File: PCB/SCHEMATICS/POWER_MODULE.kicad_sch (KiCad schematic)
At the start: 44 parts, among them Q1 PMOS, U1 C7433, U2 AMS1117-3.3, U4 AMS1117-3.3

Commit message: Added stm
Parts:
- U9: footprint (none) -> footprints:18650_Holder_SMD
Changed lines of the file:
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@@
       (effects (font (size 1.27 1.27)))
     )
-    (property "Footprint" "" (at 52.07 151.13 0)
+    (property "Footprint" "footprints:18650_Holder_SMD" (at 52.07 151.13 0)
       (effects (font (size 1.27 1.27)) hide)
     )

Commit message: Updated schematics
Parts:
- removed U9: ~, footprints:18650_Holder_SMD, symbol Battery holder:18650_holder
- Q1: footprint (none) -> footprint:SOT-23-3_L3.0-W1.6-P1.90-LS2.8-BR; PART  C20917 -> C2959854; Unit Price 0.0864 -> 0.0851
- R1, R14, R15, R4, R5, R7: PART  C17168 -> C17168
- R12: footprint (none) -> footprint:R1206
- R40: value Value: Value: Value: Value: Value: Value: 510k -> Value: Value: Value: 510k; footprint (none) -> footprint:R0402
- TP4054-42-SOT25R: footprint LIB_TP4054-42-SOT25-R:SOT95P280X100-5N -> footprint:SOT-23-5_L3.0-W1.7-P0.95-LS2.8-BL
- U1: footprint Package_TO_SOT_SMD:TSOT-23-5 -> footprint:SOIC-8_L4.9-W3.9-P1.27-LS6.0-BL
- U2, U4: footprint LIB_AMS1117-3.3:SOT229P700X180-4N -> footprint:SOT-223-4_L6.5-W3.5-P2.30-LS7.0-BR; PART  U2 -> C369933; Unit Price 0.0627 -> 0.0646
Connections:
- net GND: no longer D5.1 (K), Q1.3 (S), R10.2, R11.2, R8.1, R9.1, U1.2 (V-), U1.5 (V+)
- new net: D5.1 (K), Q1.3 (S), R10.2, R11.2, R8.1, R9.1, U1.2 (V-), U1.5 (V+)
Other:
- moved on the sheet: D3, D5, Q1, R10, R11, R12, R13, R14, R15, R40, R8, R9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

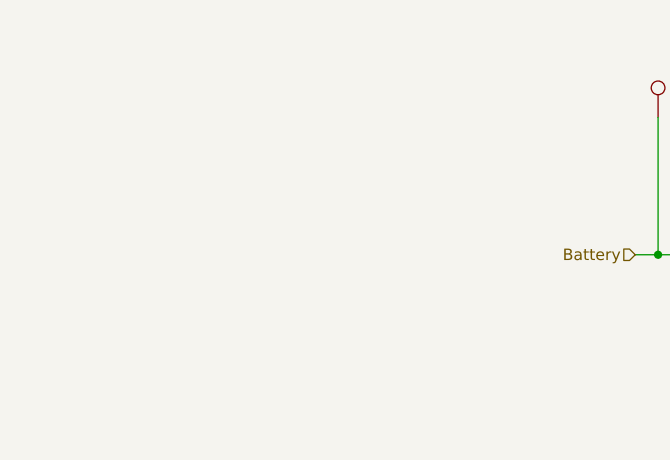
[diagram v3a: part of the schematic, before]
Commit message: Added battery
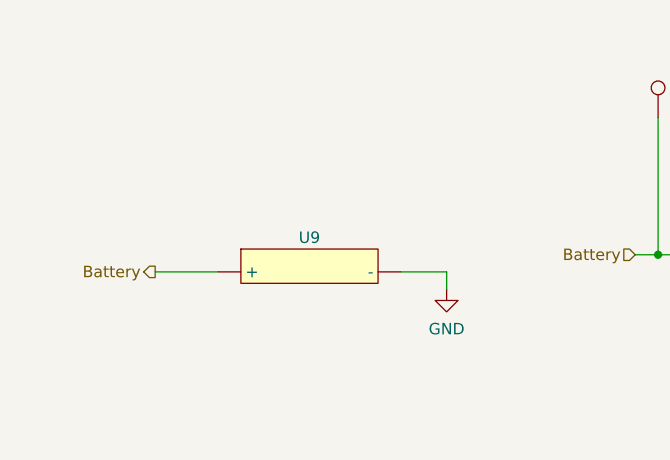
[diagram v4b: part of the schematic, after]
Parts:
- added U9: ~, footprints:18650_Holder_SMD, symbol Battery:18650
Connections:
- net Battery: now also U9. (-)
- net GND: now also U9. (-)
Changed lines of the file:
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@@
+    (stroke (width 0) (type default))
+  )
+  (wire (pts (xy 60.325 144.78) (xy 60.325 146.685))
     (stroke (width 0) (type default))
   )
@@
     (stroke (width 0) (type default))
   )
+  (wire (pts (xy 55.245 144.78) (xy 60.325 144.78))
+    (stroke (width 0) (type default))
+  )
   (wire (pts (xy 122.555 124.46) (xy 139.7 124.46))
     (stroke (width 0) (type default))
@@
   )
   (wire (pts (xy 157.48 64.77) (xy 163.83 64.77))
+    (stroke (width 0) (type default))
+  )
+  (wire (pts (xy 27.94 144.78) (xy 34.925 144.78))
     (stroke (width 0) (type default))
   )
@@
     (effects (font (size 1.27 1.27)) (justify left))
   )
+  (hierarchical_label "Battery" (shape output) (at 27.94 144.78 180) (fields_autoplaced)
+    (effects (font (size 1.27 1.27)) (justify right))
+  )
   (hierarchical_label "5V" (shape input) (at 63.5 24.13 90) (fields_autoplaced)
     (effects (font (size 1.27 1.27)) (justify left))
@@
         (path "/c9ca3a5c-30cb-4dce-b611-3270b9f3284b/c574ee02-103d-4bad-a8c0-5ec1707f609e"
           (reference "TP6") (unit 1)
+        )
+      )
+    )
+  )
+  (symbol (lib_id "Battery:18650") (at 43.815 140.97 0) (unit 1)
+    (in_bom yes) (on_board yes) (dnp no) (fields_autoplaced)
+    (property "Reference" "U9" (at 45.085 140.97 0)
+      (effects (font (size 1.27 1.27)))
+    )
+    (property "Value" "~" (at 43.815 140.97 0)
+      (effects (font (size 1.27 1.27)))
+    )
+    (property "Footprint" "footprints:18650_Holder_SMD" (at 43.815 140.97 0)
+      (effects (font (size 1.27 1.27)) hide)
+    )
+    (property "Datasheet" "" (at 43.815 140.97 0)
+      (effects (font (size 1.27 1.27)) hide)
+    )
+    (pin "")
+    (pin "")
+    (instances
+      (project "SCHEMATICS"
+        (path "/c9ca3a5c-30cb-4dce-b611-3270b9f3284b/c574ee02-103d-4bad-a8c0-5ec1707f609e"
+          (reference "U9") (unit 1)
         )
       )
@@
         )
       )
+    )
+  )
+  (symbol (lib_id "power:GND") (at 60.325 146.685 0) (unit 1)
+    (in_bom yes) (on_board yes) (dnp no) (fields_autoplaced)
+    (property "Reference" "#PWR010" (at 60.325 153.035 0)
+      (effects (font (size 1.27 1.27)) hide)
+    )
+    (property "Value" "GND" (at 60.325 151.13 0)
+      (effects (font (size 1.27 1.27)))
+    )
+    (property "Footprint" "" (at 60.325 146.685 0)
+      (effects (font (size 1.27 1.27)) hide)
+    )
+    (property "Datasheet" "" (at 60.325 146.685 0)
+      (effects (font (size 1.27 1.27)) hide)
+    )
+    (pin "1")
+    (instances
+      (project "SCHEMATICS"
+        (path "/c9ca3a5c-30cb-4dce-b611-3270b9f3284b/c574ee02-103d-4bad-a8c0-5ec1707f609e"
+          (reference "#PWR010") (unit 1)
+        )
+      )

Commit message: Fixed ercs
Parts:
- R40: value Value: Value: Value: 510k -> Value: Value: Value: Value: 510k
- TP10, TP11, TP12, TP28, TP29, TP3, TP30, TP31, TP4, TP5, TP6, TP7, TP8, TP9: footprint (none) -> TestPoint:TestPoint_Bridge_Pitch2.0mm_Drill0.7mm
- renumbered TP4054-42-SOT25R to TP4054-42-SOT25R1
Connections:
- net Battery: no longer R4.1, TP4.1, TP4054-42-SOT25R1.3 (BAT)
- new net: R4.1, TP4.1, TP4054-42-SOT25R1.3 (BAT)
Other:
- moved on the sheet: R4
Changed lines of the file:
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@@
   (junction (at 198.12 49.53) (diameter 0) (color 0 0 0 0)
   )
-  (junction (at 43.18 78.105) (diameter 0) (color 0 0 0 0)
-  )
   (junction (at 122.555 124.46) (diameter 0) (color 0 0 0 0)
   )
@@
     (stroke (width 0) (type default))
   )
-  (wire (pts (xy 43.18 69.85) (xy 43.18 78.105))
+  (wire (pts (xy 43.18 69.85) (xy 43.18 78.74))
     (stroke (width 0) (type default))
   )
@@
     (stroke (width 0) (type default))
   )
-  (wire (pts (xy 43.18 78.105) (xy 43.18 86.36))
-    (stroke (width 0) (type default))
-  )
   (wire (pts (xy 182.88 36.83) (xy 163.83 36.83))
     (stroke (width 0) (type default))
@@
     (stroke (width 0) (type default))
   )
-  (wire (pts (xy 43.18 86.36) (xy 45.72 86.36))
-    (stroke (width 0) (type default))
-  )
   (polyline (pts (xy 101.6 102.87) (xy 12.7 102.87))
     (stroke (width 0) (type default))
   )
+  (wire (pts (xy 43.18 83.82) (xy 43.18 90.805))
+    (stroke (width 0) (type default))
+  )
   (wire (pts (xy 171.45 141.605) (xy 179.07 141.605))
     (stroke (width 0) (type default))
@@
     (stroke (width 0) (type default))
   )
-  (wire (pts (xy 43.18 78.105) (xy 45.72 78.105))
-    (stroke (width 0) (type default))
-  )
   (wire (pts (xy 106.68 142.875) (xy 107.315 142.875))
     (stroke (width 0) (type default))
@@
   )
   (wire (pts (xy 210.82 115.57) (xy 210.82 124.46))
-    (stroke (width 0) (type default))
-  )
-  (wire (pts (xy 45.72 78.105) (xy 45.72 81.28))
     (stroke (width 0) (type default))
   )
@@
     (effects (font (size 1.27 1.27)) (justify right))
   )
-  (hierarchical_label "Battery" (shape output) (at 43.18 85.09 270) (fields_autoplaced)
+  (hierarchical_label "Battery" (shape output) (at 43.18 90.805 270) (fields_autoplaced)
     (effects (font (size 1.27 1.27)) (justify right))
   )
@@
       (effects (font (size 1.27 1.27)) (justify left))
     )
-    (property "Footprint" "" (at 245.11 36.83 0)
+    (property "Footprint" "TestPoint:TestPoint_Bridge_Pitch2.0mm_Drill0.7mm" (at 245.11 36.83 0)
       (effects (font (size 1.27 1.27)) hide)
     )
@@
       (effects (font (size 1.27 1.27)))
     )
-    (property "Footprint" "" (at 181.61 85.09 0)
+    (property "Footprint" "TestPoint:TestPoint_Bridge_Pitch2.0mm_Drill0.7mm" (at 181.61 85.09 0)
       (effects (font (size 1.27 1.27)) hide)
     )
@@
       (effects (font (size 1.27 1.27)) (justify left))
     )
-    (property "Footprint" "" (at 76.2 45.72 0)
+    (property "Footprint" "TestPoint:TestPoint_Bridge_Pitch2.0mm_Drill0.7mm" (at 76.2 45.72 0)
       (effects (font (size 1.27 1.27)) hide)
     )
@@
       (effects (font (size 1.27 1.27)) (justify left))
     )
-    (property "Footprint" "" (at 196.85 95.25 0)
+    (property "Footprint" "TestPoint:TestPoint_Bridge_Pitch2.0mm_Drill0.7mm" (at 196.85 95.25 0)
       (effects (font (size 1.27 1.27)) hide)
     )
@@
     )
   )
-  (symbol (lib_id "Device:R_Small_US") (at 45.72 83.82 0) (unit 1)
+  (symbol (lib_id "Device:R_Small_US") (at 43.18 81.28 0) (unit 1)
     (in_bom yes) (on_board yes) (dnp no)
-    (property "Reference" "R4" (at 44.831 78.0963 0)
-      (effects (font (size 1.27 1.27)) (justify left))
-    )
-    (property "Value" "0" (at 44.831 80.0173 0)
-      (effects (font (size 1.27 1.27)) (justify left))
-    )
-    (property "Footprint" "0ohm:RESC1005X40N" (at 45.72 83.82 0)
-      (effects (font (size 1.27 1.27)) hide)
-    )
-    (property "Datasheet" "~" (at 45.72 83.82 0)
-      (effects (font (size 1.27 1.27)) hide)
-    )
-    (property "PART " "   C17168" (at 45.72 83.82 0)
-      (effects (font (size 1.27 1.27)) hide)
-    )
-    (property "Unit Price" "0.0005" (at 45.72 83.82 0)
+    (property "Reference" "R4" (at 42.291 75.5563 0)
+      (effects (font (size 1.27 1.27)) (justify left))
+    )
+    (property "Value" "0" (at 42.291 77.4773 0)
+      (effects (font (size 1.27 1.27)) (justify left))
+    )
+    (property "Footprint" "0ohm:RESC1005X40N" (at 43.18 81.28 0)
+      (effects (font (size 1.27 1.27)) hide)
+    )
+    (property "Datasheet" "~" (at 43.18 81.28 0)
+      (effects (font (size 1.27 1.27)) hide)
+    )
+    (property "PART " "   C17168" (at 43.18 81.28 0)
+      (effects (font (size 1.27 1.27)) hide)
+    )
+    (property "Unit Price" "0.0005" (at 43.18 81.28 0)
       (effects (font (size 1.27 1.27)) hide)
     )
@@
       (effects (font (size 1.27 1.27)) (justify left))
     )
-    (property "Footprint" "" (at 189.23 102.87 0)
+    (property "Footprint" "TestPoint:TestPoint_Bridge_Pitch2.0mm_Drill0.7mm" (at 189.23 102.87 0)
       (effects (font (size 1.27 1.27)) hide)
     )
@@
       (effects (font (size 1.27 1.27)) (justify left))
     )
-    (property "Value" "Value: Value: Value:  510k" (at 124.46 141.605 0) (show_name)
+    (property "Value" "Value: Value: Value: Value:  510k" (at 124.46 141.605 0) (show_name)
       (effects (font (size 1.27 1.27)) (justify left))
     )
@@
       (effects (font (size 1.27 1.27)) (justify left))
     )
-    (property "Footprint" "" (at 215.9 115.57 0)
+    (property "Footprint" "TestPoint:TestPoint_Bridge_Pitch2.0mm_Drill0.7mm" (at 215.9 115.57 0)
       (effects (font (size 1.27 1.27)) hide)
     )
@@
       (effects (font (size 1.27 1.27)) (justify left))
     )
-    (property "Footprint" "" (at 160.02 29.21 0)
+    (property "Footprint" "TestPoint:TestPoint_Bridge_Pitch2.0mm_Drill0.7mm" (at 160.02 29.21 0)
       (effects (font (size 1.27 1.27)) hide)
     )
@@
   (symbol (lib_id "TP4054-42-SOT25-R:TP4054-42-SOT25-R") (at 55.88 64.77 0) (unit 1)
     (in_bom yes) (on_board yes) (dnp no) (fields_autoplaced)
-    (property "Reference" "TP4054-42-SOT25R" (at 71.12 61.1411 0)
+    (property "Reference" "TP4054-42-SOT25R1" (at 71.12 61.1411 0)
       (effects (font (size 1.27 1.27)))
     )
@@
       (project "SCHEMATICS"
         (path "/c9ca3a5c-30cb-4dce-b611-3270b9f3284b/c574ee02-103d-4bad-a8c0-5ec1707f609e"
-          (reference "TP4054-42-SOT25R") (unit 1)
+          (reference "TP4054-42-SOT25R1") (unit 1)
         )
       )
@@
       (effects (font (size 1.27 1.27)) (justify left))
     )
-    (property "Footprint" "" (at 175.26 30.48 0)
+    (property "Footprint" "TestPoint:TestPoint_Bridge_Pitch2.0mm_Drill0.7mm" (at 175.26 30.48 0)
       (effects (font (size 1.27 1.27)) hide)
     )
@@
       (effects (font (size 1.27 1.27)) (justify left))
     )
-    (property "Footprint" "" (at 203.2 30.48 0)
+    (property "Footprint" "TestPoint:TestPoint_Bridge_Pitch2.0mm_Drill0.7mm" (at 203.2 30.48 0)
       (effects (font (size 1.27 1.27)) hide)
     )
@@
       (effects (font (size 1.27 1.27)) (justify left))
     )
-    (property "Footprint" "" (at 146.05 29.21 0)
+    (property "Footprint" "TestPoint:TestPoint_Bridge_Pitch2.0mm_Drill0.7mm" (at 146.05 29.21 0)
       (effects (font (size 1.27 1.27)) hide)
     )
@@
       (effects (font (size 1.27 1.27)))
     )
-    (property "Footprint" "" (at 186.69 57.15 0)
+    (property "Footprint" "TestPoint:TestPoint_Bridge_Pitch2.0mm_Drill0.7mm" (at 186.69 57.15 0)
       (effects (font (size 1.27 1.27)) hide)
     )
@@
       (effects (font (size 1.27 1.27)) (justify left))
     )
-    (property "Footprint" "" (at 76.2 55.88 0)
+    (property "Footprint" "TestPoint:TestPoint_Bridge_Pitch2.0mm_Drill0.7mm" (at 76.2 55.88 0)
       (effects (font (size 1.27 1.27)) hide)
     )
@@
       (effects (font (size 1.27 1.27)) (justify right))
     )
-    (property "Footprint" "" (at 45.72 80.01 0)
+    (property "Footprint" "TestPoint:TestPoint_Bridge_Pitch2.0mm_Drill0.7mm" (at 45.72 80.01 0)
       (effects (font (size 1.27 1.27)) hide)
     )
@@
       (effects (font (size 1.27 1.27)) (justify left))
     )
-    (property "Footprint" "" (at 88.9 127.635 0)
-      (effects (font (size 1.27 1.27)) hide)
-    )
+    (property "Footprint" "TestPoint:TestPoint_Bridge_Pitch2.0mm_Drill0.7mm" (at 88.9 127.635 0)
+      (effects (font (size 1.27 1.27)) hide)
+    )

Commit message: Fixing ERCs
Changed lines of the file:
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@@
     (effects (font (size 1.27 1.27)) (justify left bottom))
   )
-  (hierarchical_label "UVLO Output" (shape input) (at 127.635 49.53 180) (fields_autoplaced)
-    (effects (font (size 1.27 1.27)) (justify right))
+  (label "UVLO Output" (at 127.635 49.53 180) (fields_autoplaced)
+    (effects (font (size 1.27 1.27)) (justify right bottom))
+  )
+  (label "UVLO Output" (at 214.63 124.46 0) (fields_autoplaced)
+    (effects (font (size 1.27 1.27)) (justify left bottom))
   )
   (hierarchical_label "Battery" (shape output) (at 43.18 90.805 270) (fields_autoplaced)
@@
     (effects (font (size 1.27 1.27)) (justify left))
   )
-  (hierarchical_label "UVLO Output" (shape input) (at 214.63 124.46 0) (fields_autoplaced)
-    (effects (font (size 1.27 1.27)) (justify left))
-  )

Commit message: Fixing ERCs
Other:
- note added: "Battery connector (not populated)"
- moved on the sheet: D3, D5, Q1, R10, R11, R12, R13, R14, R15, R40, R8, R9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

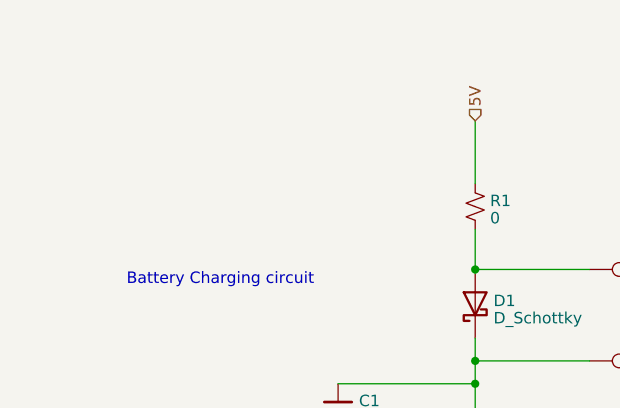
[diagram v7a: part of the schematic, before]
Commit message: Added pwr flags
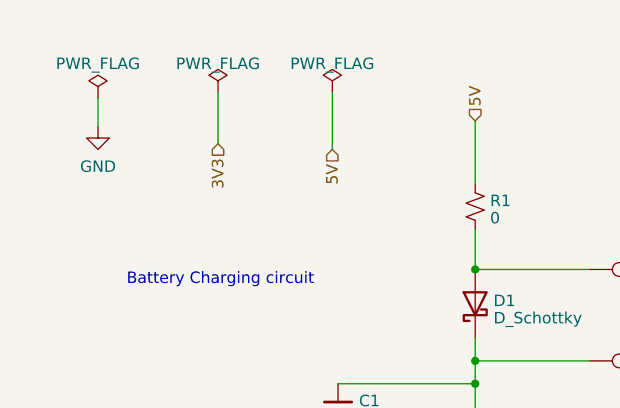
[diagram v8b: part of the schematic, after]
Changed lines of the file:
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@@
+    (stroke (width 0) (type default))
+  )
+  (wire (pts (xy 47.625 20.955) (xy 47.625 27.305))
     (stroke (width 0) (type default))
   )
@@
     (stroke (width 0) (type default))
   )
+  (wire (pts (xy 34.925 20.955) (xy 34.925 26.67))
+    (stroke (width 0) (type default))
+  )
   (wire (pts (xy 172.72 132.715) (xy 172.72 135.255))
     (stroke (width 0) (type default))
@@
   )
   (wire (pts (xy 189.865 137.16) (xy 189.865 142.875))
+    (stroke (width 0) (type default))
+  )
+  (wire (pts (xy 21.59 21.59) (xy 21.59 24.765))
     (stroke (width 0) (type default))
   )
@@
   (hierarchical_label "5V" (shape input) (at 63.5 24.13 90) (fields_autoplaced)
     (effects (font (size 1.27 1.27)) (justify left))
+  )
+  (hierarchical_label "3V3" (shape input) (at 34.925 26.67 270) (fields_autoplaced)
+    (effects (font (size 1.27 1.27)) (justify right))
+  )
+  (hierarchical_label "5V" (shape input) (at 47.625 27.305 270) (fields_autoplaced)
+    (effects (font (size 1.27 1.27)) (justify right))
   )
   (symbol (lib_id "Connector:TestPoint") (at 240.03 36.83 0) (unit 1)
@@
     )
   )
+  (symbol (lib_id "power:GND") (at 21.59 24.765 0) (unit 1)
+    (in_bom yes) (on_board yes) (dnp no) (fields_autoplaced)
+    (property "Reference" "#PWR018" (at 21.59 31.115 0)
+      (effects (font (size 1.27 1.27)) hide)
+    )
+    (property "Value" "GND" (at 21.59 29.21 0)
+      (effects (font (size 1.27 1.27)))
+    )
+    (property "Footprint" "" (at 21.59 24.765 0)
+      (effects (font (size 1.27 1.27)) hide)
+    )
+    (property "Datasheet" "" (at 21.59 24.765 0)
+      (effects (font (size 1.27 1.27)) hide)
+    )
+    (pin "1")
+    (instances
+      (project "SCHEMATICS"
+        (path "/c9ca3a5c-30cb-4dce-b611-3270b9f3284b/c574ee02-103d-4bad-a8c0-5ec1707f609e"
+          (reference "#PWR018") (unit 1)
+        )
+      )
+    )
+  )
   (symbol (lib_id "Device:R_Small_US") (at 229.235 133.985 0) (unit 1)
     (in_bom yes) (on_board yes) (dnp no) (fields_autoplaced)
@@
     )
   )
+  (symbol (lib_id "power:PWR_FLAG") (at 47.625 20.955 0) (unit 1)
+    (in_bom yes) (on_board yes) (dnp no) (fields_autoplaced)
+    (property "Reference" "#FLG03" (at 47.625 19.05 0)
+      (effects (font (size 1.27 1.27)) hide)
+    )
+    (property "Value" "PWR_FLAG" (at 47.625 17.78 0)
+      (effects (font (size 1.27 1.27)))
+    )
+    (property "Footprint" "" (at 47.625 20.955 0)
+      (effects (font (size 1.27 1.27)) hide)
+    )
+    (property "Datasheet" "~" (at 47.625 20.955 0)
+      (effects (font (size 1.27 1.27)) hide)
+    )
+    (pin "1")
+    (instances
+      (project "SCHEMATICS"
+        (path "/c9ca3a5c-30cb-4dce-b611-3270b9f3284b/c574ee02-103d-4bad-a8c0-5ec1707f609e"
+          (reference "#FLG03") (unit 1)
+        )
+      )
+    )
+  )
   (symbol (lib_id "Device:R_Small_US") (at 157.48 57.15 0) (unit 1)
     (in_bom yes) (on_board yes) (dnp no)
@@
         )
       )
+    )
+  )
+  (symbol (lib_id "power:PWR_FLAG") (at 34.925 20.955 0) (unit 1)
+    (in_bom yes) (on_board yes) (dnp no) (fields_autoplaced)
+    (property "Reference" "#FLG02" (at 34.925 19.05 0)
+      (effects (font (size 1.27 1.27)) hide)
+    )
+    (property "Value" "PWR_FLAG" (at 34.925 17.78 0)
+      (effects (font (size 1.27 1.27)))
+    )
+    (property "Footprint" "" (at 34.925 20.955 0)
+      (effects (font (size 1.27 1.27)) hide)
+    )
+    (property "Datasheet" "~" (at 34.925 20.955 0)
+      (effects (font (size 1.27 1.27)) hide)
+    )
+    (pin "1")
+    (instances
+      (project "SCHEMATICS"
+        (path "/c9ca3a5c-30cb-4dce-b611-3270b9f3284b/c574ee02-103d-4bad-a8c0-5ec1707f609e"
+          (reference "#FLG02") (unit 1)
+        )
+      )
+    )
+  )
+  (symbol (lib_id "power:PWR_FLAG") (at 21.59 21.59 0) (unit 1)
+    (in_bom yes) (on_board yes) (dnp no) (fields_autoplaced)
+    (property "Reference" "#FLG01" (at 21.59 19.685 0)
+      (effects (font (size 1.27 1.27)) hide)
+    )
+    (property "Value" "PWR_FLAG" (at 21.59 17.78 0)
+      (effects (font (size 1.27 1.27)))
+    )
+    (property "Footprint" "" (at 21.59 21.59 0)
+      (effects (font (size 1.27 1.27)) hide)
+    )
+    (property "Datasheet" "~" (at 21.59 21.59 0)
+      (effects (font (size 1.27 1.27)) hide)
+    )
+    (pin "1")
+    (instances
+      (project "SCHEMATICS"
+        (path "/c9ca3a5c-30cb-4dce-b611-3270b9f3284b/c574ee02-103d-4bad-a8c0-5ec1707f609e"
+          (reference "#FLG01") (unit 1)
+        )
+      )
